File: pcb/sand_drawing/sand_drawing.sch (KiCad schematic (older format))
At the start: 19 parts, among them J0 12VDC, J1 Stepper1, J10 Driver 1 M0, J11 Driver 1 M1, J12 Driver 1 M2, J2 Stepper2, J3 Arm 1 Opto, J4 Arm 2 Opto, J5 ESP POWER, J6 Unused Pins, J7 Driver 2 M0, J8 Driver 2 M1, J9 Driver 2 M2, U1 WeMos_D1_mini, U2 LD1117_TO220

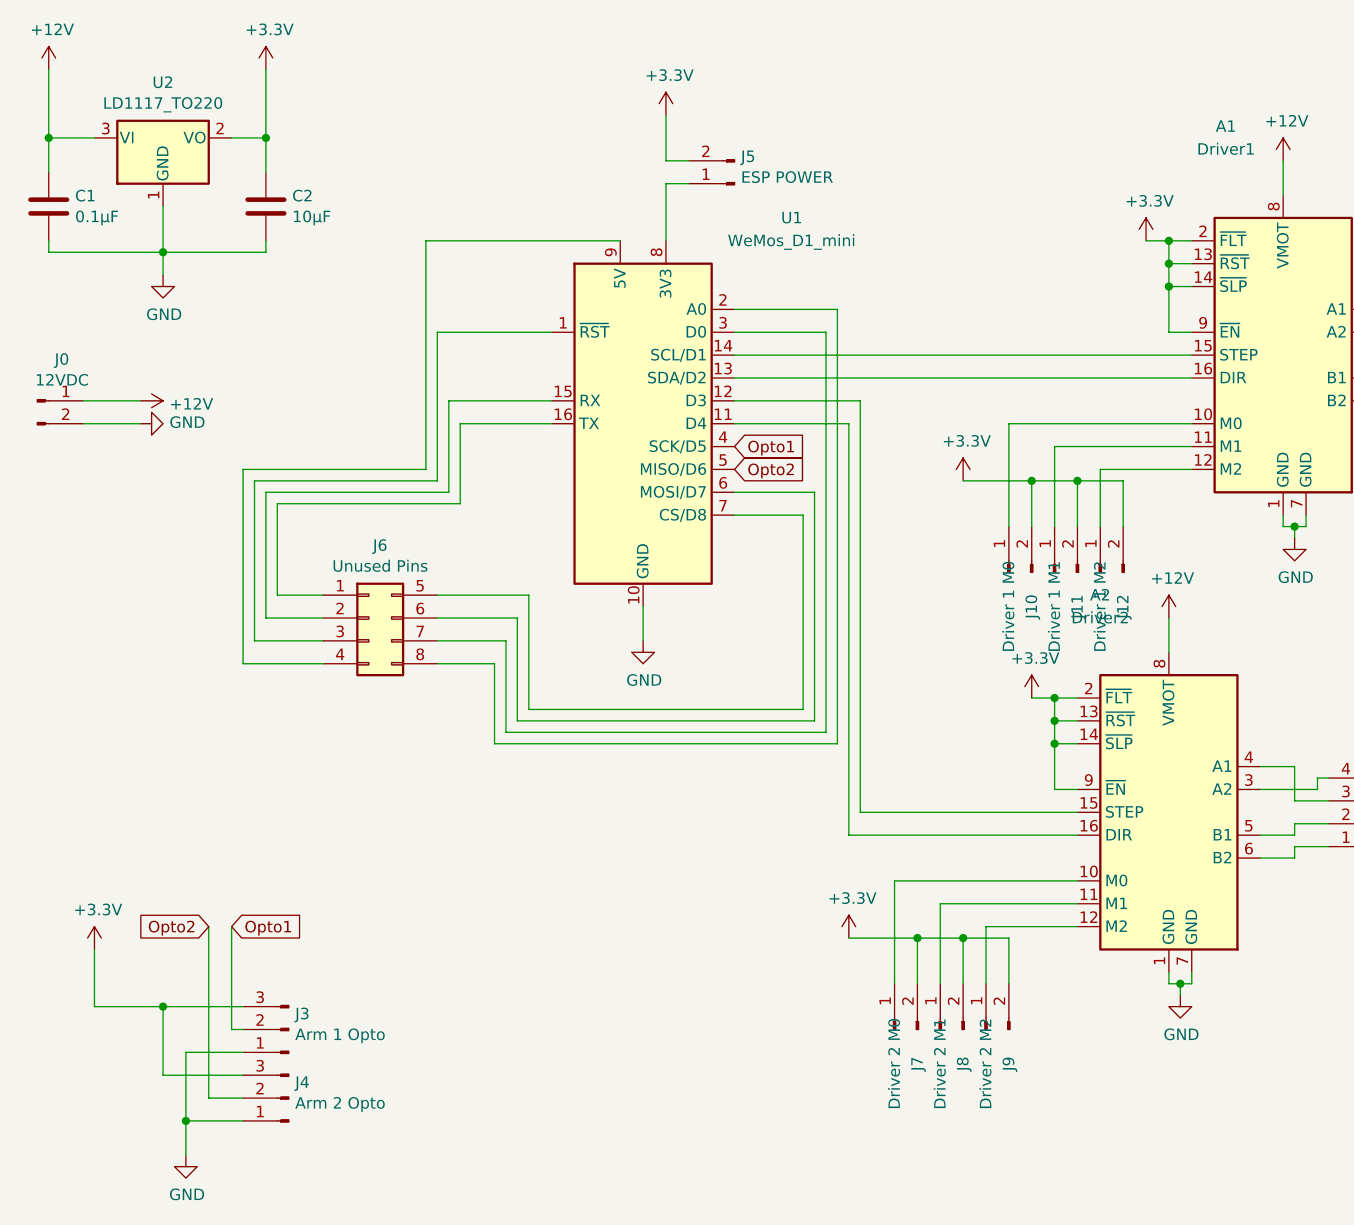
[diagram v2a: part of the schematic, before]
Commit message: Add flood fills.
Add silkscreen text for spare pins.
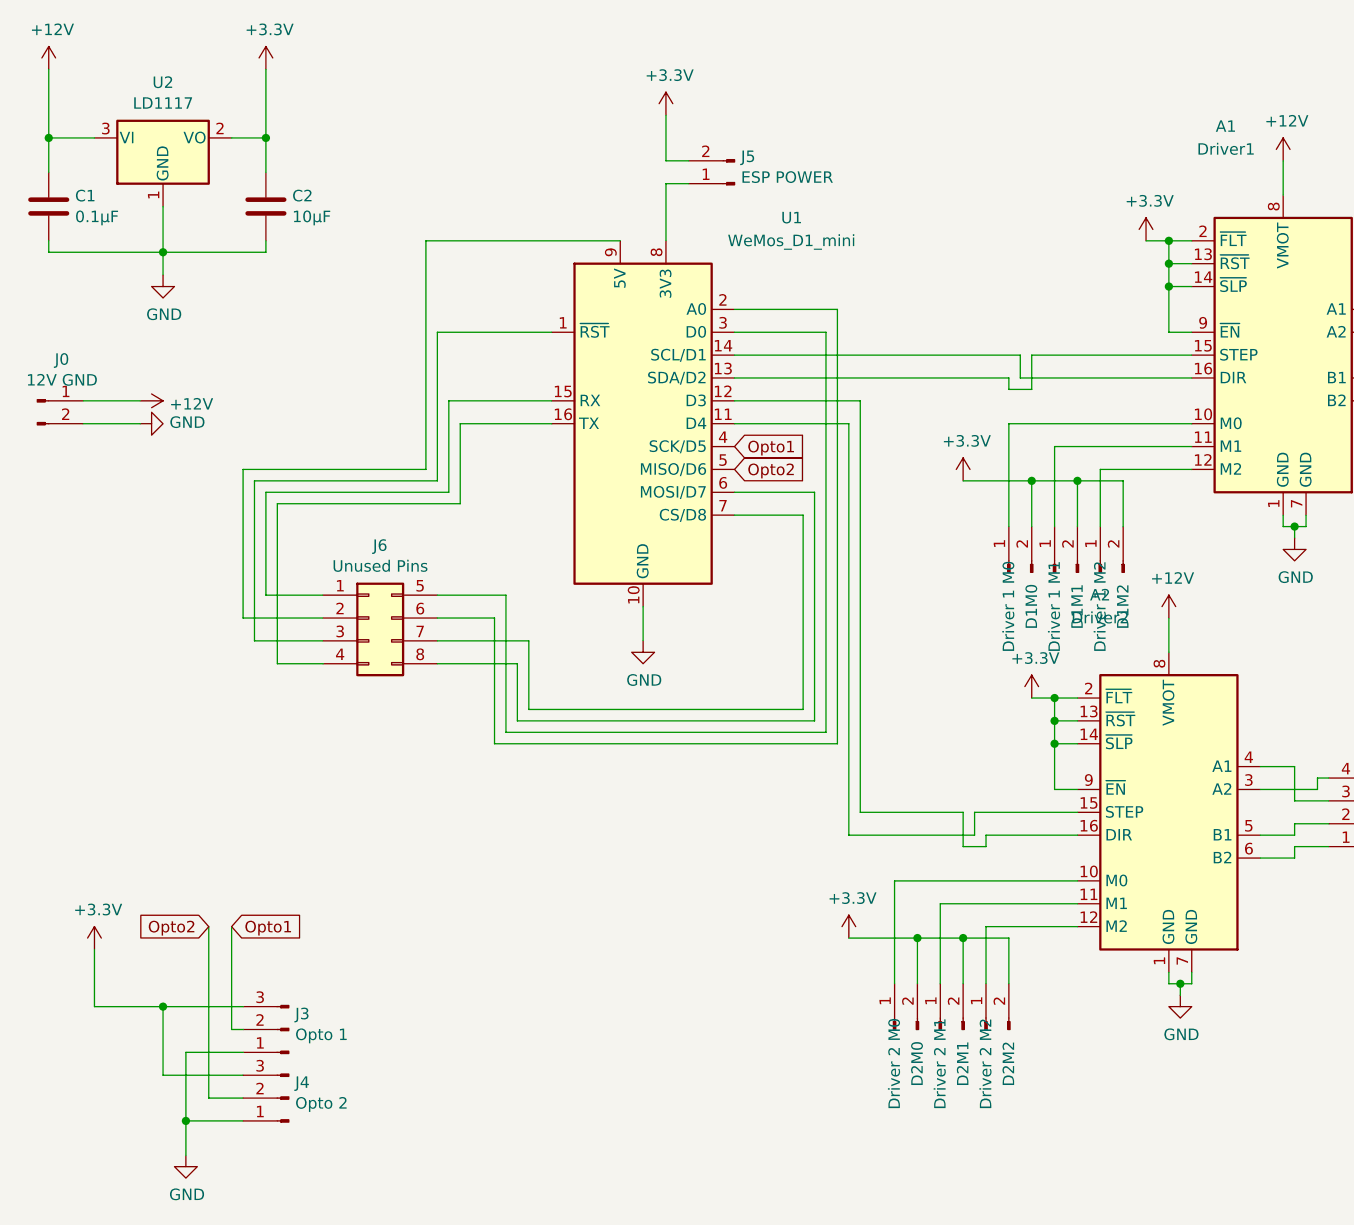
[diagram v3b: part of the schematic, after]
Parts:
- J0: value 12VDC -> 12V GND
- J3: value Arm 1 Opto -> Opto 1
- J4: value Arm 2 Opto -> Opto 2
- U2: value LD1117_TO220 -> LD1117
- renumbered J10 to D1M0, J11 to D1M1, J12 to D1M2, J7 to D2M0, J8 to D2M1, J9 to D2M2
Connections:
- net at U1.11 (D4): now also A2.15 (STEP); no longer A2.16 (DIR)
- net at U1.12 (D3): now also A2.16 (DIR); no longer A2.15 (STEP)
- net at U1.13 (SDA/D2): now also A1.15 (STEP); no longer A1.16 (DIR)
- net at U1.14 (SCL/D1): now also A1.16 (DIR); no longer A1.15 (STEP)
- net at U1.15 (RX): now also J6.1 (Pin_1); no longer J6.2 (Pin_2)
- net at U1.16 (TX): now also J6.4 (Pin_4); no longer J6.1 (Pin_1)
- net at U1.2 (A0): now also J6.6 (Pin_6); no longer J6.8 (Pin_8)
- net at U1.3 (D0): now also J6.5 (Pin_5); no longer J6.7 (Pin_7)
- net at U1.6 (MOSI/D7): now also J6.8 (Pin_8); no longer J6.6 (Pin_6)
- net at U1.7 (CS/D8): now also J6.7 (Pin_7); no longer J6.5 (Pin_5)
- net at U1.9 (5V): now also J6.2 (Pin_2); no longer J6.4 (Pin_4)
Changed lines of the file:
@@
 P 1750 5250
 F 0 "J3" H 1722 5182 50  0000 R CNN
-F 1 "Arm 1 Opto" H 1722 5273 50  0000 R CNN
+F 1 "Opto 1" H 1722 5273 50  0000 R CNN
 F 2 "Socket_Strips:Socket_Strip_Straight_1x03_Pitch2.54mm" H 1750 5250 50  0001 C CNN
 F 3 "~" H 1750 5250 50  0001 C CNN
@@
 P 1750 5550
 F 0 "J4" H 1722 5482 50  0000 R CNN
-F 1 "Arm 2 Opto" H 1722 5573 50  0000 R CNN
+F 1 "Opto 2" H 1722 5573 50  0000 R CNN
 F 2 "Socket_Strips:Socket_Strip_Straight_1x03_Pitch2.54mm" H 1750 5550 50  0001 C CNN
 F 3 "~" H 1750 5550 50  0001 C CNN
@@
 P 1200 1350
 F 0 "U2" H 1200 1592 50  0000 C CNN
-F 1 "LD1117_TO220" H 1200 1501 50  0000 C CNN
+F 1 "LD1117" H 1200 1501 50  0000 C CNN
 F 2 "Power_Integrations:TO-220" H 1200 1575 50  0001 C CIN
 F 3 "http://www.fairchildsemi.com/ds/LM/LM7805.pdf" H 1200 1300 50  0001 C CNN
@@
 P 650 2500
 F 0 "J0" H 758 2681 50  0000 C CNN
-F 1 "12VDC" H 758 2590 50  0000 C CNN
+F 1 "12V GND" H 758 2590 50  0000 C CNN
 F 2 "Socket_Strips:Socket_Strip_Straight_1x02_Pitch2.54mm" H 650 2500 50  0001 C CNN
 F 3 "~" H 650 2500 50  0001 C CNN
@@
 	2350 2800 1550 2800
 Wire Wire Line
-	1550 2800 1550 3650
-Wire Wire Line
-	1550 3650 1900 3650
+	1550 2800 1550 3450
 Wire Wire Line
 	2900 2200 2400 2200
@@
 	2400 2200 2400 2850
 Wire Wire Line
-	2400 2850 1600 2850
-Wire Wire Line
 	1600 2850 1600 3550
 Wire Wire Line
@@
 	2450 2900 1650 2900
 Wire Wire Line
-	1650 2900 1650 3450
-Wire Wire Line
-	1650 3450 1900 3450
-Wire Wire Line
 	2900 2600 2500 2600
 Wire Wire Line
@@
 	2500 2950 1700 2950
 Wire Wire Line
-	1700 2950 1700 3350
-Wire Wire Line
-	1700 3350 1900 3350
-Wire Wire Line
 	3700 3000 4000 3000
 Wire Wire Line
@@
 	4000 3850 2800 3850
 Wire Wire Line
-	2800 3850 2800 3350
-Wire Wire Line
-	2800 3350 2400 3350
+	2800 3850 2800 3550
 Wire Wire Line
 	3700 2900 4050 2900
@@
 	4050 2900 4050 3900
 Wire Wire Line
-	4050 3900 2750 3900
-Wire Wire Line
-	2750 3900 2750 3450
-Wire Wire Line
-	2750 3450 2400 3450
-Wire Wire Line
 	3700 2200 4100 2200
 Wire Wire Line
@@
 	4100 3950 2700 3950
 Wire Wire Line
-	2700 3950 2700 3550
-Wire Wire Line
-	2700 3550 2400 3550
-Wire Wire Line
 	3700 2100 4150 2100
 Wire Wire Line
@@
 Wire Wire Line
 	4150 4000 2650 4000
-Wire Wire Line
-	2650 4000 2650 3650
-Wire Wire Line
-	2650 3650 2400 3650
-$Comp
-L Connector:Conn_01x02_Male J7
-U 1 1 5E99CB34
-P 4400 5250
-F 0 "J7" H 4250 5150 50  0000 C CNN
-F 1 "Driver 2 M0" H 4250 5250 50  0000 C CNN
-F 2 "Socket_Strips:Socket_Strip_Straight_1x02_Pitch2.54mm" H 4400 5250 50  0001 C CNN
-F 3 "~" H 4400 5250 50  0001 C CNN
-	1    4400 5250
-	0    -1   -1   0
-$EndComp
-$Comp
-L Connector:Conn_01x02_Male J8
+$Comp
+L Connector:Conn_01x02_Male D2M1
 U 1 1 5E9C5CF2
 P 4600 5250
-F 0 "J8" H 4450 5150 50  0000 C CNN
+F 0 "D2M1" H 4450 5150 50  0000 C CNN
 F 1 "Driver 2 M1" H 4450 5250 50  0000 C CNN
 F 2 "Socket_Strips:Socket_Strip_Straight_1x02_Pitch2.54mm" H 4600 5250 50  0001 C CNN
@@
 $EndComp
 $Comp
-L Connector:Conn_01x02_Male J9
+L Connector:Conn_01x02_Male D2M2
 U 1 1 5E9C5F13
 P 4800 5250
-F 0 "J9" H 4650 5150 50  0000 C CNN
+F 0 "D2M2" H 4650 5150 50  0000 C CNN
 F 1 "Driver 2 M2" H 4650 5250 50  0000 C CNN
 F 2 "Socket_Strips:Socket_Strip_Straight_1x02_Pitch2.54mm" H 4800 5250 50  0001 C CNN
@@
 	4250 4300 4250 2500
 Wire Wire Line
-	4250 4300 5200 4300
-Wire Wire Line
-	4200 4400 5200 4400
-Wire Wire Line
 	5200 4600 4400 4600
 Wire Wire Line
@@
 	4200 4850 4500 4850
 Wire Wire Line
-	3700 2300 5700 2300
-Wire Wire Line
-	3700 2400 5700 2400
-Wire Wire Line
 	6100 1450 6100 1600
 Wire Wire Line
 	5600 3600 5600 3450
 $Comp
-L Connector:Conn_01x02_Male J10
+L Connector:Conn_01x02_Male D1M0
 U 1 1 5EA4E3CF
 P 4900 3250
-F 0 "J10" H 4750 3150 50  0000 C CNN
+F 0 "D1M0" H 4750 3150 50  0000 C CNN
 F 1 "Driver 1 M0" H 4750 3250 50  0000 C CNN
 F 2 "Socket_Strips:Socket_Strip_Straight_1x02_Pitch2.54mm" H 4900 3250 50  0001 C CNN
@@
 $EndComp
 $Comp
-L Connector:Conn_01x02_Male J11
+L Connector:Conn_01x02_Male D1M1
 U 1 1 5EA4E3D5
 P 5100 3250
-F 0 "J11" H 4950 3150 50  0000 C CNN
+F 0 "D1M1" H 4950 3150 50  0000 C CNN
 F 1 "Driver 1 M1" H 4950 3250 50  0000 C CNN
 F 2 "Socket_Strips:Socket_Strip_Straight_1x02_Pitch2.54mm" H 5100 3250 50  0001 C CNN
@@
 $EndComp
 $Comp
-L Connector:Conn_01x02_Male J12
+L Connector:Conn_01x02_Male D1M2
 U 1 1 5EA4E3DB
 P 5300 3250
-F 0 "J12" H 5150 3150 50  0000 C CNN
+F 0 "D1M2" H 5150 3150 50  0000 C CNN
 F 1 "Driver 1 M2" H 5150 3250 50  0000 C CNN
 F 2 "Socket_Strips:Socket_Strip_Straight_1x02_Pitch2.54mm" H 5300 3250 50  0001 C CNN
@@
 Wire Wire Line
 	5100 2700 5700 2700
+Wire Wire Line
+	5700 2400 4950 2400
+Wire Wire Line
+	4950 2400 4950 2300
+Wire Wire Line
+	4950 2300 3700 2300
+Wire Wire Line
+	5700 2300 5000 2300
+Wire Wire Line
+	5000 2300 5000 2450
+Wire Wire Line
+	5000 2450 4900 2450
+Wire Wire Line
+	4900 2450 4900 2400
+Wire Wire Line
+	4900 2400 3700 2400
+Wire Wire Line
+	4800 4400 5200 4400
+Wire Wire Line
+	4750 4300 4750 4400
+Wire Wire Line
+	4200 4400 4750 4400
+Wire Wire Line
+	4750 4300 5200 4300
+Wire Wire Line
+	4700 4300 4700 4450
+Wire Wire Line
+	4700 4450 4800 4450
+Wire Wire Line
+	4800 4450 4800 4400
+Wire Wire Line
+	4250 4300 4700 4300
+$Comp
+L Connector:Conn_01x02_Male D2M0
+U 1 1 5E99CB34
+P 4400 5250
+F 0 "D2M0" H 4250 5150 50  0000 C CNN
+F 1 "Driver 2 M0" H 4250 5250 50  0000 C CNN
+F 2 "Socket_Strips:Socket_Strip_Straight_1x02_Pitch2.54mm" H 4400 5250 50  0001 C CNN
+F 3 "~" H 4400 5250 50  0001 C CNN
+	1    4400 5250
+	0    -1   -1   0
+$EndComp
+Wire Wire Line
+	4050 3900 2750 3900
+Wire Wire Line
+	2650 3450 2650 4000
+Wire Wire Line
+	2650 3450 2400 3450
+Wire Wire Line
+	2750 3650 2750 3900
+Wire Wire Line
+	2400 3650 2750 3650
+Wire Wire Line
+	2400 3550 2800 3550
+Wire Wire Line
+	2700 3950 2700 3350
+Wire Wire Line
+	2700 3350 2400 3350
+Wire Wire Line
+	1650 2900 1650 3350
+Wire Wire Line
+	1650 3350 1900 3350
+Wire Wire Line
+	2400 2850 1600 2850
+Wire Wire Line
+	1700 2950 1700 3650
+Wire Wire Line
+	1700 3650 1900 3650
+Wire Wire Line
+	1900 3450 1550 3450
 $EndSCHEMATC

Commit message: Tidy up schematic.
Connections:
- net D2Step: now reaches A2.15 (STEP), U1.11 (D4)
- net D2Dir: now reaches A2.16 (DIR), U1.12 (D3)
- net D1Step: now reaches A1.15 (STEP), U1.13 (SDA/D2)
- net D1Dir: now reaches A1.16 (DIR), U1.14 (SCL/D1)
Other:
- moved on the sheet: A1, D1M0, D1M1, D1M2, J1
